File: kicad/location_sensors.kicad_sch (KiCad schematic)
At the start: 0 parts

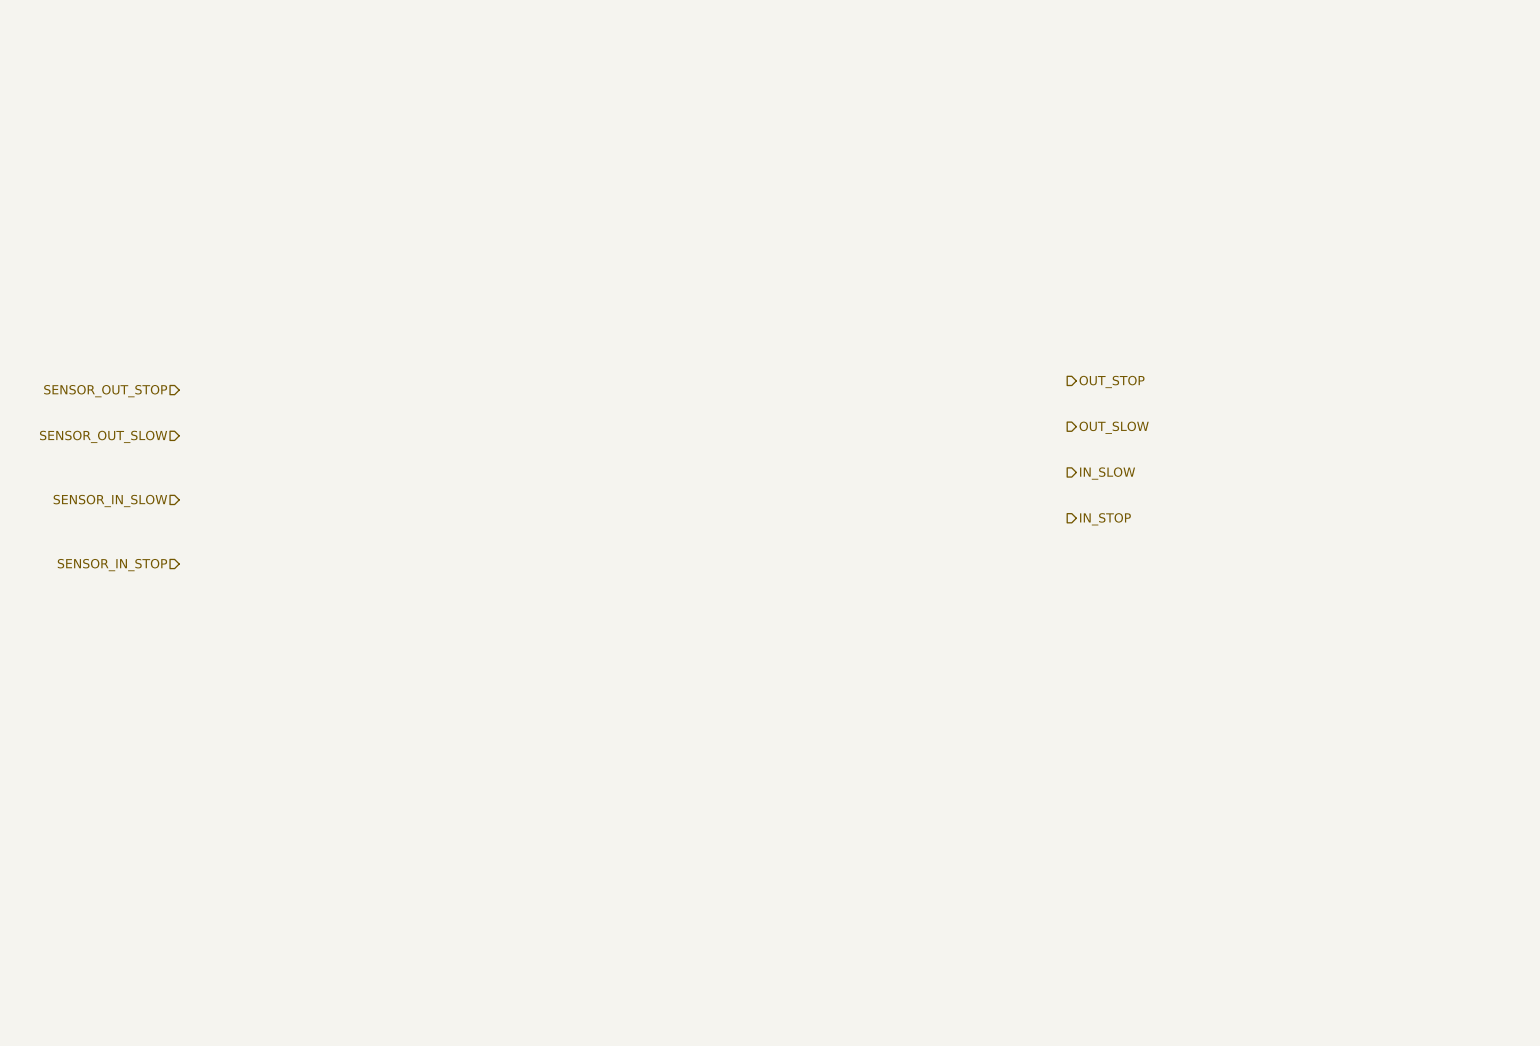
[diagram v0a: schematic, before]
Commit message: Completed the schematic. All components have Digikey part numbers and footprints. The power supply sheet still requires some work.
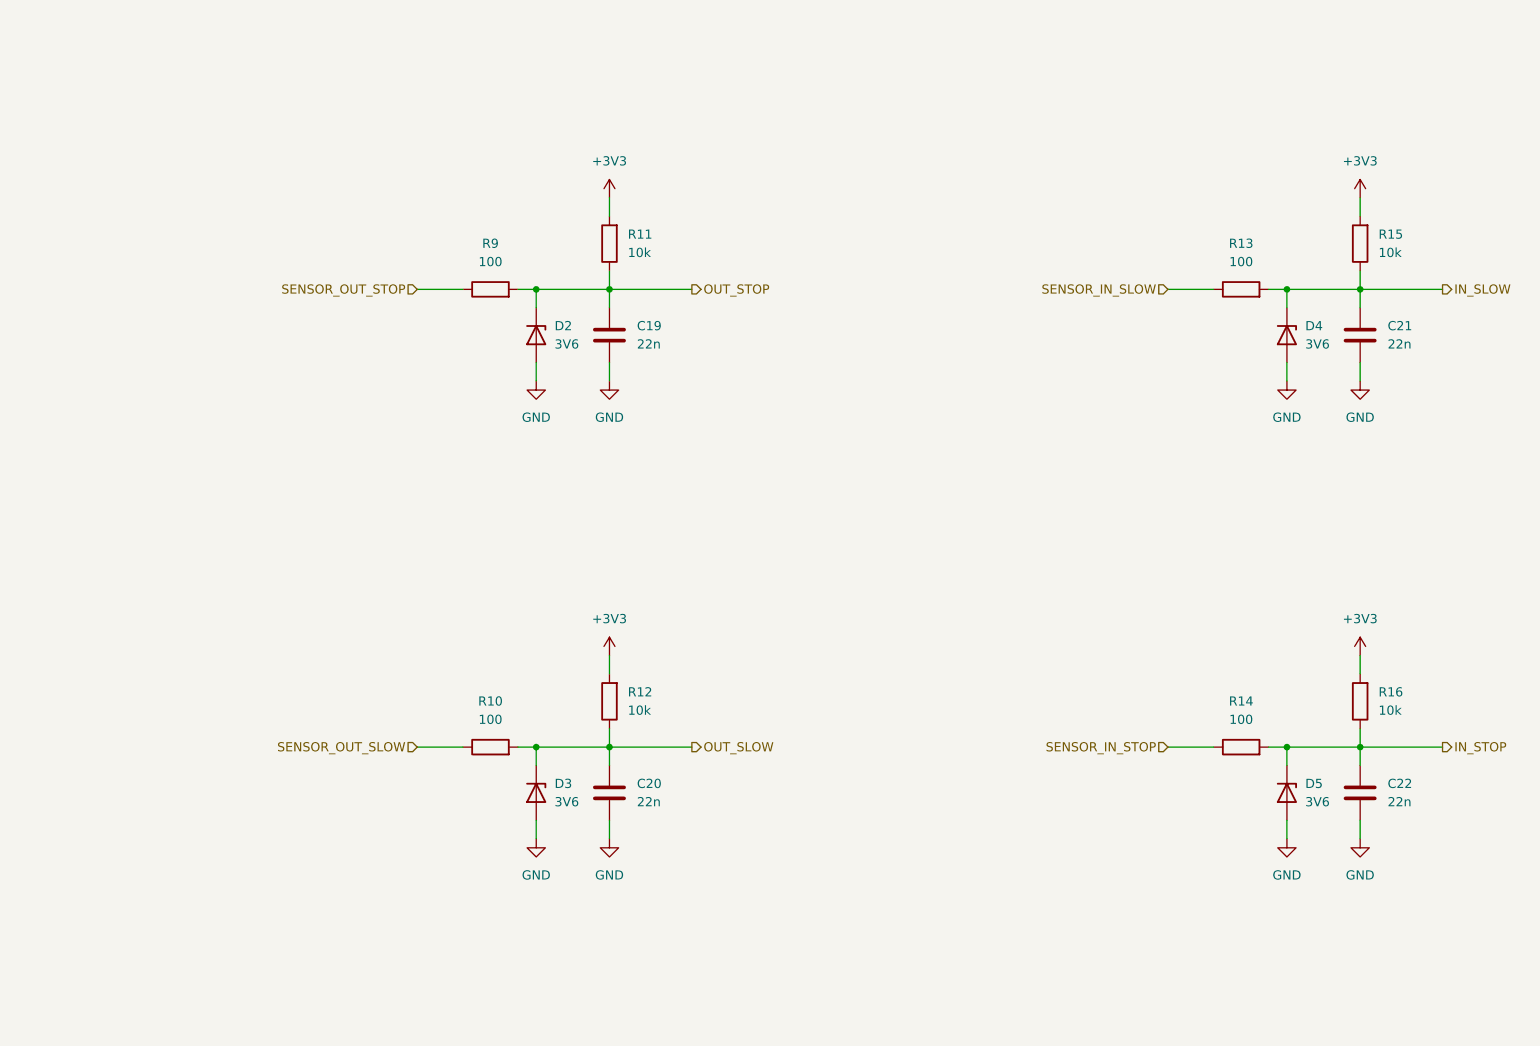
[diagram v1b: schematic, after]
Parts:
- added C19, C20, C21, C22: 22n, Capacitor_SMD:C_0603_1608Metric, symbol Device:C
- added D2, D3, D4, D5: 3V6, Diode_SMD:D_SOD-123, symbol Device:D_Zener
- added R10, R13, R14, R9: 100, Resistor_SMD:R_0603_1608Metric, symbol Device:R
- added R11, R12, R15, R16: 10k, Resistor_SMD:R_0603_1608Metric, symbol Device:R
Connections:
- net IN_SLOW: now also C21.1, D4.1 (K), R13.2, R15.1
- net IN_STOP: now also C22.1, D5.1 (K), R14.2, R16.1
- net OUT_SLOW: now also C20.1, D3.1 (K), R10.2, R12.1
- net OUT_STOP: now also C19.1, D2.1 (K), R11.1, R9.2
- net SENSOR_IN_SLOW: now also R13.1
- net SENSOR_IN_STOP: now also R14.1
- net SENSOR_OUT_SLOW: now also R10.1
- net SENSOR_OUT_STOP: now also R9.1
- new net +3V3: R11.2, R12.2, R15.2, R16.2
- new net GND: C19.2, C20.2, C21.2, C22.2, D2.2 (A), D3.2 (A), D4.2 (A), D5.2 (A)
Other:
- company: (none) -> NX Solutions
- title: (none) -> TV slider

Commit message: Updated footprints and step models. Placed on PCB, but not yet positioned in final location.
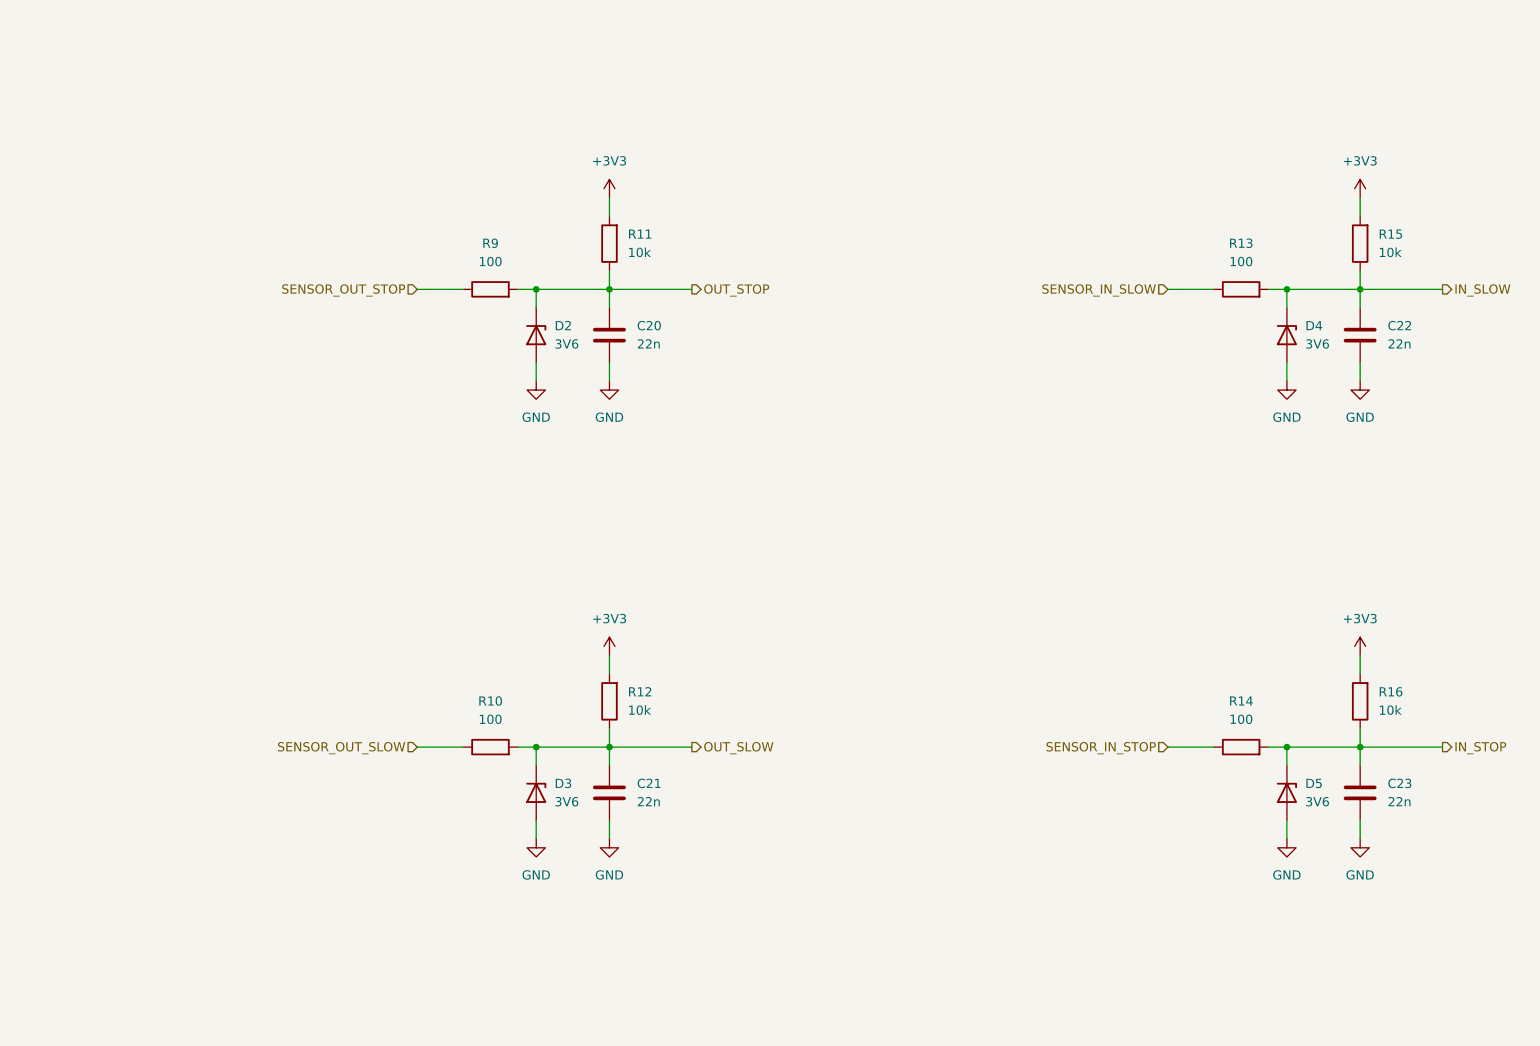
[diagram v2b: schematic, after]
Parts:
- renumbered C19 to C20, C20 to C21, C21 to C22, C22 to C23
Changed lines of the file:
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@@
 		(dnp no)
 		(fields_autoplaced yes)
-		(property "Reference" "C20"
+		(property "Reference" "C21"
 			(at 107.95 124.4599 0)
 			(effects
@@
 			(project "tv_slider"
 				(path "/914c4b67-a7a4-47f3-8515-668040fd3f8c/816aa5cb-6066-4d97-997e-6fcfac1c1c32"
-					(reference "C20")
+					(reference "C21")
 					(unit 1)
 				)
@@
 		(dnp no)
 		(fields_autoplaced yes)
-		(property "Reference" "#PWR062"
+		(property "Reference" "#PWR065"
 			(at 208.28 74.93 0)
 			(effects
@@
 			(project "tv_slider"
 				(path "/914c4b67-a7a4-47f3-8515-668040fd3f8c/816aa5cb-6066-4d97-997e-6fcfac1c1c32"
-					(reference "#PWR062")
+					(reference "#PWR065")
 					(unit 1)
 				)
@@
 		(dnp no)
 		(fields_autoplaced yes)
-		(property "Reference" "C21"
+		(property "Reference" "C22"
 			(at 212.09 60.9599 0)
 			(effects
@@
 			(project "tv_slider"
 				(path "/914c4b67-a7a4-47f3-8515-668040fd3f8c/816aa5cb-6066-4d97-997e-6fcfac1c1c32"
-					(reference "C21")
+					(reference "C22")
 					(unit 1)
 				)
@@
 		(dnp no)
 		(fields_autoplaced yes)
-		(property "Reference" "#PWR053"
+		(property "Reference" "#PWR056"
 			(at 93.98 74.93 0)
 			(effects
@@
 			(project ""
 				(path "/914c4b67-a7a4-47f3-8515-668040fd3f8c/816aa5cb-6066-4d97-997e-6fcfac1c1c32"
-					(reference "#PWR053")
+					(reference "#PWR056")
 					(unit 1)
 				)
@@
 		(dnp no)
 		(fields_autoplaced yes)
-		(property "Reference" "#PWR056"
+		(property "Reference" "#PWR059"
 			(at 104.14 74.93 0)
 			(effects
@@
 			(project "tv_slider"
 				(path "/914c4b67-a7a4-47f3-8515-668040fd3f8c/816aa5cb-6066-4d97-997e-6fcfac1c1c32"
-					(reference "#PWR056")
+					(reference "#PWR059")
 					(unit 1)
 				)
@@
 		(dnp no)
 		(fields_autoplaced yes)
-		(property "Reference" "#PWR059"
+		(property "Reference" "#PWR062"
 			(at 198.12 74.93 0)
 			(effects
@@
 			(project "tv_slider"
 				(path "/914c4b67-a7a4-47f3-8515-668040fd3f8c/816aa5cb-6066-4d97-997e-6fcfac1c1c32"
-					(reference "#PWR059")
+					(reference "#PWR062")
 					(unit 1)
 				)
@@
 		(dnp no)
 		(fields_autoplaced yes)
-		(property "Reference" "C19"
+		(property "Reference" "C20"
 			(at 107.95 60.9599 0)
 			(effects
@@
 			(project ""
 				(path "/914c4b67-a7a4-47f3-8515-668040fd3f8c/816aa5cb-6066-4d97-997e-6fcfac1c1c32"
-					(reference "C19")
+					(reference "C20")
 					(unit 1)
 				)
@@
 		(dnp no)
 		(fields_autoplaced yes)
-		(property "Reference" "#PWR057"
+		(property "Reference" "#PWR060"
 			(at 104.14 110.49 0)
 			(effects
@@
 			(project "tv_slider"
 				(path "/914c4b67-a7a4-47f3-8515-668040fd3f8c/816aa5cb-6066-4d97-997e-6fcfac1c1c32"
-					(reference "#PWR057")
+					(reference "#PWR060")
 					(unit 1)
 				)
@@
 		(dnp no)
 		(fields_autoplaced yes)
-		(property "Reference" "#PWR060"
+		(property "Reference" "#PWR063"
 			(at 198.12 138.43 0)
 			(effects
@@
 			(project "tv_slider"
 				(path "/914c4b67-a7a4-47f3-8515-668040fd3f8c/816aa5cb-6066-4d97-997e-6fcfac1c1c32"
-					(reference "#PWR060")
+					(reference "#PWR063")
 					(unit 1)
 				)
@@
 		(dnp no)
 		(fields_autoplaced yes)
-		(property "Reference" "#PWR058"
+		(property "Reference" "#PWR061"
 			(at 104.14 138.43 0)
 			(effects
@@
 			(project "tv_slider"
 				(path "/914c4b67-a7a4-47f3-8515-668040fd3f8c/816aa5cb-6066-4d97-997e-6fcfac1c1c32"
-					(reference "#PWR058")
+					(reference "#PWR061")
 					(unit 1)
 				)
@@
 		(dnp no)
 		(fields_autoplaced yes)
-		(property "Reference" "#PWR055"
+		(property "Reference" "#PWR058"
 			(at 104.14 46.99 0)
 			(effects
@@
 			(project ""
 				(path "/914c4b67-a7a4-47f3-8515-668040fd3f8c/816aa5cb-6066-4d97-997e-6fcfac1c1c32"
-					(reference "#PWR055")
+					(reference "#PWR058")
 					(unit 1)
 				)
@@
 		(dnp no)
 		(fields_autoplaced yes)
-		(property "Reference" "#PWR054"
+		(property "Reference" "#PWR057"
 			(at 93.98 138.43 0)
 			(effects
@@
 			(project "tv_slider"
 				(path "/914c4b67-a7a4-47f3-8515-668040fd3f8c/816aa5cb-6066-4d97-997e-6fcfac1c1c32"
-					(reference "#PWR054")
+					(reference "#PWR057")
 					(unit 1)
 				)
@@
 		(dnp no)
 		(fields_autoplaced yes)
-		(property "Reference" "#PWR063"
+		(property "Reference" "#PWR066"
 			(at 208.28 110.49 0)
 			(effects
@@
 			(project "tv_slider"
 				(path "/914c4b67-a7a4-47f3-8515-668040fd3f8c/816aa5cb-6066-4d97-997e-6fcfac1c1c32"
-					(reference "#PWR063")
+					(reference "#PWR066")
 					(unit 1)
 				)
@@
 		(dnp no)
 		(fields_autoplaced yes)
-		(property "Reference" "#PWR061"
+		(property "Reference" "#PWR064"
 			(at 208.28 46.99 0)
 			(effects
@@
 			(project "tv_slider"
 				(path "/914c4b67-a7a4-47f3-8515-668040fd3f8c/816aa5cb-6066-4d97-997e-6fcfac1c1c32"
-					(reference "#PWR061")
+					(reference "#PWR064")
 					(unit 1)
 				)
@@
 		(dnp no)
 		(fields_autoplaced yes)
-		(property "Reference" "#PWR064"
+		(property "Reference" "#PWR067"
 			(at 208.28 138.43 0)
 			(effects
@@
 			(project "tv_slider"
 				(path "/914c4b67-a7a4-47f3-8515-668040fd3f8c/816aa5cb-6066-4d97-997e-6fcfac1c1c32"
-					(reference "#PWR064")
+					(reference "#PWR067")
 					(unit 1)
 				)
@@
 		(dnp no)
 		(fields_autoplaced yes)
-		(property "Reference" "C22"
+		(property "Reference" "C23"
 			(at 212.09 124.4599 0)
 			(effects
@@
 			(project "tv_slider"
 				(path "/914c4b67-a7a4-47f3-8515-668040fd3f8c/816aa5cb-6066-4d97-997e-6fcfac1c1c32"
-					(reference "C22")
-					(unit 1)
-				)
+					(reference "C23")
+					(unit 1)
+				)

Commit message: Updated all schematic pages except the power supply. Did the initial component placement.
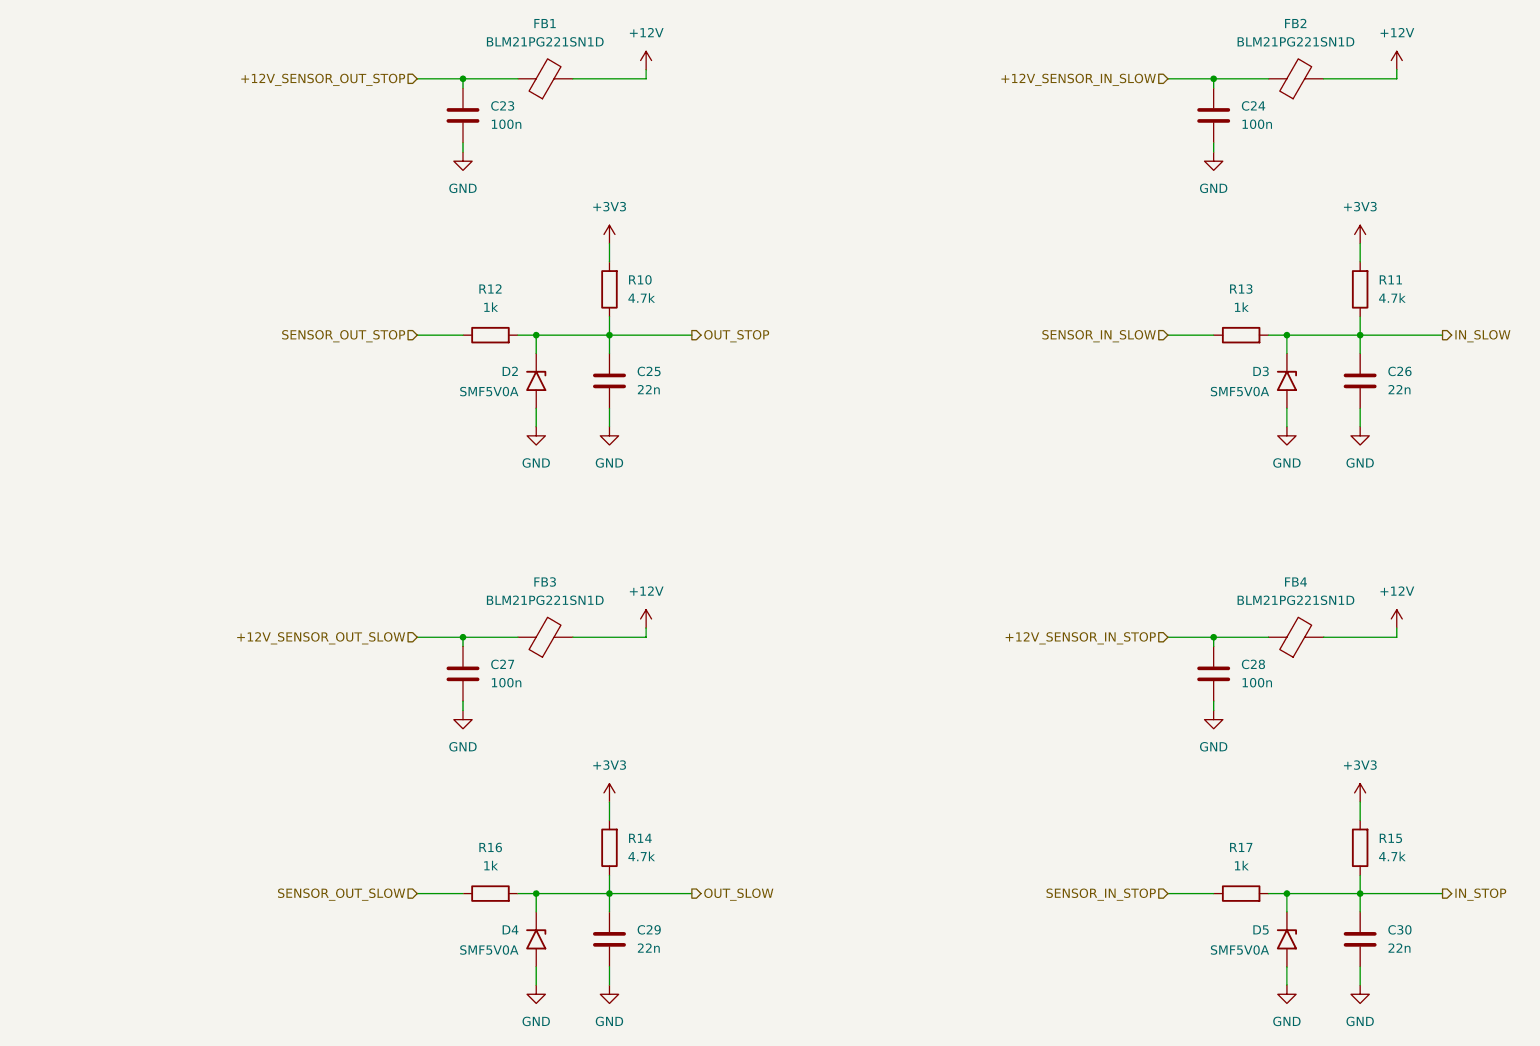
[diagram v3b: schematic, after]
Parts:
- removed D2, D3, D4, D5: 3V6, Diode_SMD:D_SOD-123, symbol Device:D_Zener
- added C23, C24, C27, C28: 100n, Capacitor_SMD:C_0603_1608Metric, symbol Device:C
- added D2, D3, D4, D5: SMF5V0A, Diode_SMD:D_SMF, symbol Diode:SMF5V0A
- added FB1, FB2, FB3, FB4: BLM21PG221SN1D, Inductor_SMD:L_0805_2012Metric, symbol Device:FerriteBead
- R10: renamed from R11; value 10k -> 4.7k; MP RC0603FR-0710KL -> RC0603FR-074K7L; SupplierPN 311-10.0KHRCT-ND -> 311-4.70KHRCT-ND
- R11: renamed from R15; value 10k -> 4.7k; MP RC0603FR-0710KL -> RC0603FR-074K7L; SupplierPN 311-10.0KHRCT-ND -> 311-4.70KHRCT-ND
- R12: renamed from R9; value 100 -> 1k; MP RC0603FR-07100RL -> RC0603FR-071KL; SupplierPN 311-100GRTR-ND -> 311-1.00KHRCT-ND
- R13: value 100 -> 1k; MP RC0603FR-07100RL -> RC0603FR-071KL; SupplierPN 311-100GRTR-ND -> 311-1.00KHRCT-ND
- R14: renamed from R12; value 10k -> 4.7k; MP RC0603FR-0710KL -> RC0603FR-074K7L; SupplierPN 311-10.0KHRCT-ND -> 311-4.70KHRCT-ND
- R15: renamed from R16; value 10k -> 4.7k; MP RC0603FR-0710KL -> RC0603FR-074K7L; SupplierPN 311-10.0KHRCT-ND -> 311-4.70KHRCT-ND
- R16: renamed from R10; value 100 -> 1k; MP RC0603FR-07100RL -> RC0603FR-071KL; SupplierPN 311-100GRTR-ND -> 311-1.00KHRCT-ND
- R17: renamed from R14; value 100 -> 1k; MP RC0603FR-07100RL -> RC0603FR-071KL; SupplierPN 311-100GRTR-ND -> 311-1.00KHRCT-ND
- renumbered C20 to C25, C22 to C26, C21 to C29, C23 to C30
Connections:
- net GND: now also C23.2, C24.2, C27.2, C28.2, D2.2 (A2), D3.2 (A2), D4.2 (A2), D5.2 (A2)
- net IN_SLOW: now also D3.1 (A1)
- net IN_STOP: now also D5.1 (A1)
- net OUT_SLOW: now also D4.1 (A1)
- net OUT_STOP: now also D2.1 (A1)
- new net +12V: FB1.2, FB2.2, FB3.2, FB4.2
- new net +12V_SENSOR_IN_SLOW: C24.1, FB2.1
- new net +12V_SENSOR_IN_STOP: C28.1, FB4.1
- new net +12V_SENSOR_OUT_SLOW: C27.1, FB3.1
- new net +12V_SENSOR_OUT_STOP: C23.1, FB1.1
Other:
- moved on the sheet: C25, C26, C29, C30, R10, R11, R12, R13, R14, R15, R16, R17
